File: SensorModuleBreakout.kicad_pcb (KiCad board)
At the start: 2 copper layers, 41 x 42.7 mm, 23 parts, among them J1 Conn_01x04, J2 Conn_ST_STDC14, J3 Conn_01x03, J4 Conn_01x10, J5 Conn_01x15, U1 STM32U031C8Tx

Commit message: V2
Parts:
- removed FB1: 120R, Inductor_SMD:L_0603_1608Metric
- removed S1: USEQGSEAC82180, USEQGS:USEQGSEAC82180
- added C10: 100n, Capacitor_SMD:C_0402_1005Metric, F.Cu at (130.5, 65.0)
- added C12: 100n, Capacitor_SMD:C_0402_1005Metric, F.Cu at (135.9, 93.2)
- added C9: 100n, Capacitor_SMD:C_0402_1005Metric, F.Cu at (124.9, 60.6)
- added H1: MountingHole_Pad, MountingHole:MountingHole_3.2mm_M3_DIN965_Pad, F.Cu at (106.0, 56.0)
- added H2: MountingHole_Pad, MountingHole:MountingHole_3.2mm_M3_DIN965_Pad, F.Cu at (154.0, 56.0)
- added H3: MountingHole_Pad, MountingHole:MountingHole_3.2mm_M3_DIN965_Pad, F.Cu at (106.0, 104.0)
- added H4: MountingHole_Pad, MountingHole:MountingHole_3.2mm_M3_DIN965_Pad, F.Cu at (154.0, 104.0)
- added R4: 2M, Resistor_SMD:R_0603_1608Metric, F.Cu at (118.0, 90.3)
- added R5: 1M, Resistor_SMD:R_0402_1005Metric, F.Cu at (118.0, 92.9)
- added R6: 220r, Resistor_SMD:R_0402_1005Metric, F.Cu at (120.5, 97.1)
- added REF**: ToolingHole_1.152mm, MountingHole:ToolingHole_1.152mm, F.Cu at (157.2, 62.0)
- added REF**: ToolingHole_1.152mm, MountingHole:ToolingHole_1.152mm, F.Cu at (103.1, 61.9)
- added REF**: ToolingHole_1.152mm, MountingHole:ToolingHole_1.152mm, F.Cu at (156.9, 97.5)
- added U2: SHT4x, Sensor_Humidity:Sensirion_DFN-4_1.5x1.5mm_P0.8mm_SHT4x_NoCentralPad, F.Cu at (124.9, 62.4)
- added U3: STC31-C-R3, STC31_C_R3:XDCR_STC31-C-R3, F.Cu at (130.0, 62.0)
- added U4: LPS22DF, Package_LGA:ST_HLGA-10_2x2mm_P0.5mm_LayoutBorder3x2y, F.Cu at (135.3, 62.4)
- C5: value 10n -> 100n
- C6: value 1u -> 10n
- C8: value 100n -> 1u
- D1: footprint LED_SMD:LED_0402_1005Metric -> LED_SMD:LED_0603_1608Metric
- J1: value Conn_01x04 -> Conn_ST_STDC14; footprint Connector_JST:JST_XH_B4B-XH-A_1x04_P2.50mm_Vertical -> Connector_PinHeader_1.27mm:PinHeader_2x07_P1.27mm_Vertical
- J2: value Conn_ST_STDC14 -> Conn_01x10; footprint Connector_PinHeader_1.27mm:PinHeader_2x07_P1.27mm_Vertical_SMD -> Connector_PinHeader_2.54mm:PinHeader_1x10_P2.54mm_Vertical
- J3: value Conn_01x03 -> Conn_01x15; footprint Connector_JST:JST_XH_B3B-XH-A_1x03_P2.50mm_Vertical -> Connector_PinHeader_2.54mm:PinHeader_1x15_P2.54mm_Vertical
- J4: value Conn_01x10 -> Conn_01x03; footprint Connector_PinHeader_2.54mm:PinHeader_1x10_P2.54mm_Vertical -> Connector_JST:JST_XH_B3B-XH-A_1x03_P2.50mm_Vertical
- J5: value Conn_01x15 -> Conn_01x04; footprint Connector_PinHeader_2.54mm:PinHeader_1x15_P2.54mm_Vertical -> Connector_JST:JST_XH_B4B-XH-A_1x04_P2.50mm_Vertical
- JP1: value JP -> Jumper_2_Open
- JP2: value Jumper_2_Open -> JP
- R1, R2, R3: value 1k5 -> 10k
- moved J3 75.1 mm to (154.0, 61.9)
- moved J4 48.5 mm to (113.7, 104.0)
- moved J1 41.9 mm to (140.4, 105.2), turned to 90 degrees
- moved J5 40.8 mm to (126.9, 104.1)
- moved R3 38.3 mm to (131.0, 78.9), turned to 180 degrees
- moved JP2 32.4 mm to (120.3, 99.5)
- moved C6 31.2 mm to (125.2, 89.1), turned to 90 degrees
- moved C7 30.3 mm to (124.0, 89.1), turned to 90 degrees
- moved C1 28.4 mm to (127.8, 81.3)
- moved C2 28.2 mm to (128.2, 82.7)
- moved U1 28.0 mm to (131.0, 88.5)
- moved C4 28.0 mm to (133.9, 94.2)
- moved C3 28.0 mm to (136.8, 85.5)
- moved C5 27.5 mm to (125.2, 84.9)
- moved D1 26.8 mm to (118.1, 97.1)
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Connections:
- C11 pad 1: Net-(S1-CAP) -> +3V3
- C5 pad 1: +3V3A -> +3V3
- C6 pad 1: +3V3A -> +3V3
- C8 pad 1: VBAT -> +3V3
- J1 pad 1: TX -> unconnected-(J1-NC-Pad1)
- J1 pad 2: RX -> unconnected-(J1-NC-Pad2)
- J1 pad 3: WKE -> +3V3
- J1 pad 4: RDY -> JTMS/SWDIO
- J2 pad 1: unconnected-(J2-NC-Pad1) -> +3V3
- J2 pad 10: unconnected-(J2-JTDI/NC-Pad10) -> PA1
- J2 pad 2: unconnected-(J2-NC-Pad2) -> GND
- J2 pad 3: +3V3 -> PB4
- J2 pad 4: JTMS/SWDIO -> PA15
- J2 pad 5: GND -> PA12
- J2 pad 6: JTCK_SWCLK -> PA11
- J2 pad 7: GND -> PB8
- J2 pad 8: JTDO/SWO -> PB9
- J2 pad 9: unconnected-(J2-JRCLK/NC-Pad9) -> PA8
- J3 pad 1: VBAT -> SDA
- J3 pad 2: GND -> SCL
- J3 pad 3: +3V3 -> PB15
- J4 pad 1: +3V3 -> VBAT
- J4 pad 3: PB8 -> +3V3
- J5 pad 1: +3V3 -> CC_TX
- J5 pad 2: GND -> CC_RX
- J5 pad 3: unconnected-(J5-Pin_3-Pad3) -> CC_WKE
- J5 pad 4: PA8 -> CC_RDY
- JP1 pad 1: Net-(JP1-A) -> +3V3
- JP1 pad 2: +3V3 -> /BOOT0
- JP2 pad 1: +3V3 -> Net-(JP2-A)
- JP2 pad 2: VBAT -> +3V3
- R1 pad 1: +3V3 -> /BOOT0
- R1 pad 2: SCL -> GND
- R2 pad 2: SDA -> SCL
- R3 pad 1: Net-(D1-A) -> +3V3
- R3 pad 2: Net-(JP1-A) -> SDA
- U1 pad 1: VBAT -> +3V3
- U1 pad 10: PA0 -> Net-(U1-PA0)
- U1 pad 12: TX -> CC_TX
- U1 pad 13: RX -> CC_RX
- U1 pad 14: WKE -> CC_WKE
- U1 pad 15: RDY -> CC_RDY
- U1 pad 2: PC13 -> unconnected-(U1-PC13-Pad2)
- U1 pad 3: PC14 -> unconnected-(U1-PC14-Pad3)
- U1 pad 30: SCL -> VCP_TX
- U1 pad 31: SDA -> VCP_RX
- U1 pad 32: INT -> PA11
- U1 pad 33: CS -> PA12
- U1 pad 38: unconnected-(U1-PA15-Pad38) -> PA15
- U1 pad 4: PC15 -> unconnected-(U1-PC15-Pad4)
- U1 pad 40: unconnected-(U1-PB4-Pad40) -> PB4
- U1 pad 41: unconnected-(U1-PB5-Pad41) -> INT
- U1 pad 42: VCP_TX -> SCL
- U1 pad 43: VCP_RX -> SDA
- U1 pad 44: unconnected-(U1-PF3-Pad44) -> /BOOT0
- U1 pad 5: PF0 -> unconnected-(U1-PF0-Pad5)
- U1 pad 9: +3V3A -> +3V3
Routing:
- net +3V3: track 256.7 -> 30.0 mm, vias 4 -> 11
- net SDA: track 8.18 -> 66.7 mm
- net SCL: track 11.6 -> 64.1 mm, vias 0 -> 3
- net PA15: track 0.00 -> 40.4 mm, vias 0 -> 1
- net PB4: track 0.00 -> 39.8 mm, vias 0 -> 2
- net PA11: track 0.00 -> 36.3 mm
- net PA12: track 0.00 -> 35.9 mm, vias 0 -> 3
- net /BOOT0: track 0.00 -> 33.6 mm, vias 0 -> 2
- net NRST: track 64.1 -> 30.8 mm
- net JTDO/SWO: track 10.5 -> 34.7 mm, vias 0 -> 1
- net VCP_RX: track 15.8 -> 39.2 mm, vias 0 -> 2
- net VCP_TX: track 11.5 -> 34.7 mm, vias 0 -> 2
- net VBAT: track 38.9 -> 17.5 mm, vias 2 -> 0
- net JTCK_SWCLK: track 10.4 -> 31.4 mm, vias 0 -> 1
- net PB14: track 19.9 -> 39.0 mm, vias 0 -> 2
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- added copper zone on In2.Cu, net +3V3
- added copper zone on In1.Cu, net GND
- removed copper zone on B.Cu, net GND
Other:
- board size 41 x 42.7 mm -> 60 x 60 mm
- copper layers 2 -> 4
- board text added: "CottonCandy"
- board text added: "PA11"
- board text added: "PA12"
- board text added: "PA15"
- board text added: "PA6"
- board text added: "PB4"
- board text added: "SCL"
- board text added: "SDA"
- board text added: "Temp, Humidity, Pressure, CO2 Sensor Module"
- board text added: "UART1_RX"
- board text added: "UART1_TX"
- board text removed: "+"
- board text removed: "-"
- board text removed: "NC"
- board text removed: "PA0"
- board text removed: "PC13"
- board text removed: "PC14"
- board text removed: "PC15"
- board text removed: "PF0"
- board text removed: "PWR LED"
- board text removed: "STMU0 Sensor Module"
- board text removed: "VBAT Short"

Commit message: update
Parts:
- removed U4: LPS22DF, Package_LGA:ST_HLGA-10_2x2mm_P0.5mm_LayoutBorder3x2y
- added U5: MS5607-02BA, Package_LGA:LGA-8_3x5mm_P1.25mm, F.Cu at (136.2, 61.7)
- moved C11 1.82 mm to (133.8, 61.8), turned to -90 degrees
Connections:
- U1 pad 41: INT -> unconnected-(U1-PB5-Pad41)
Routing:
- net INT: track 25.8 -> 0.00 mm, vias 2 -> 0
- net SCL: track 64.1 -> 68.4 mm
- net SDA: track 66.7 -> 68.7 mm
- net GND: track 32.4 -> 34.3 mm, vias 20 -> 21
- net +3V3: track 30.0 -> 29.1 mm

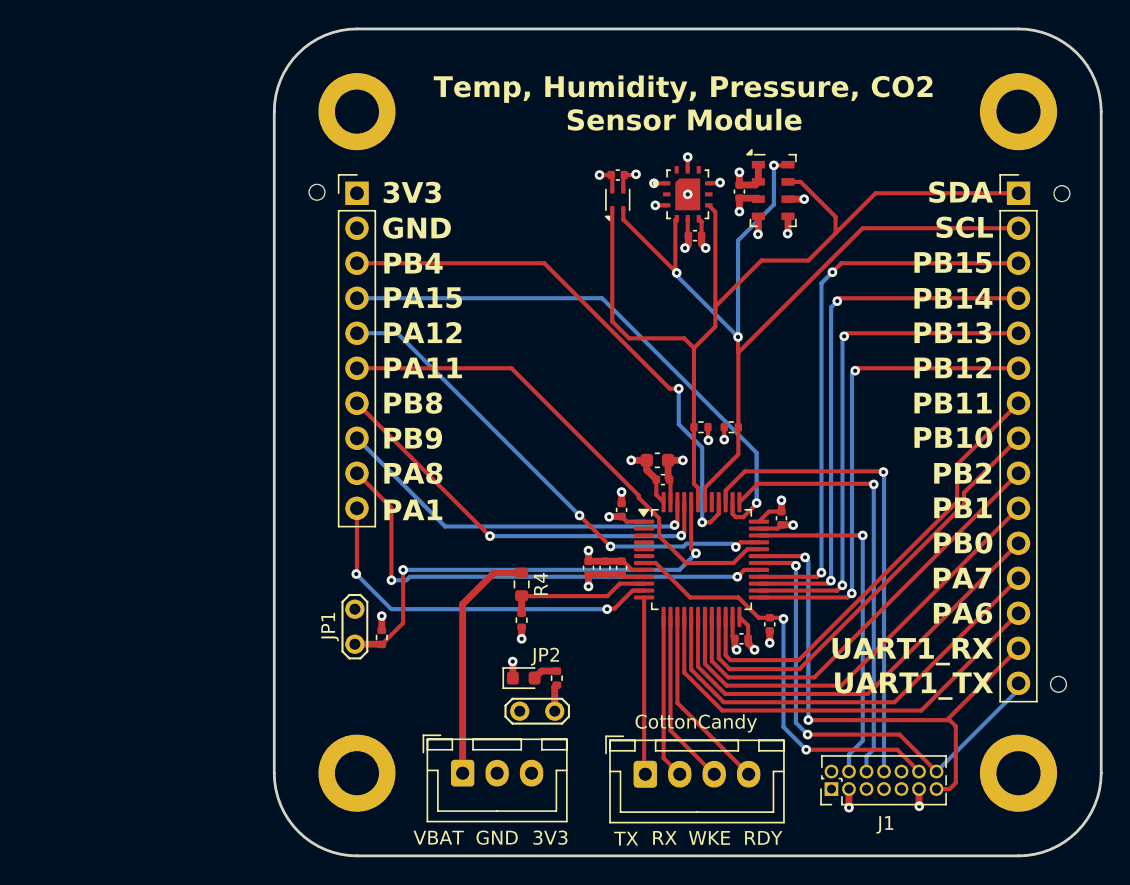
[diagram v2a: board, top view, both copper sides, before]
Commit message: Fix some rotation errors and minor cleanup
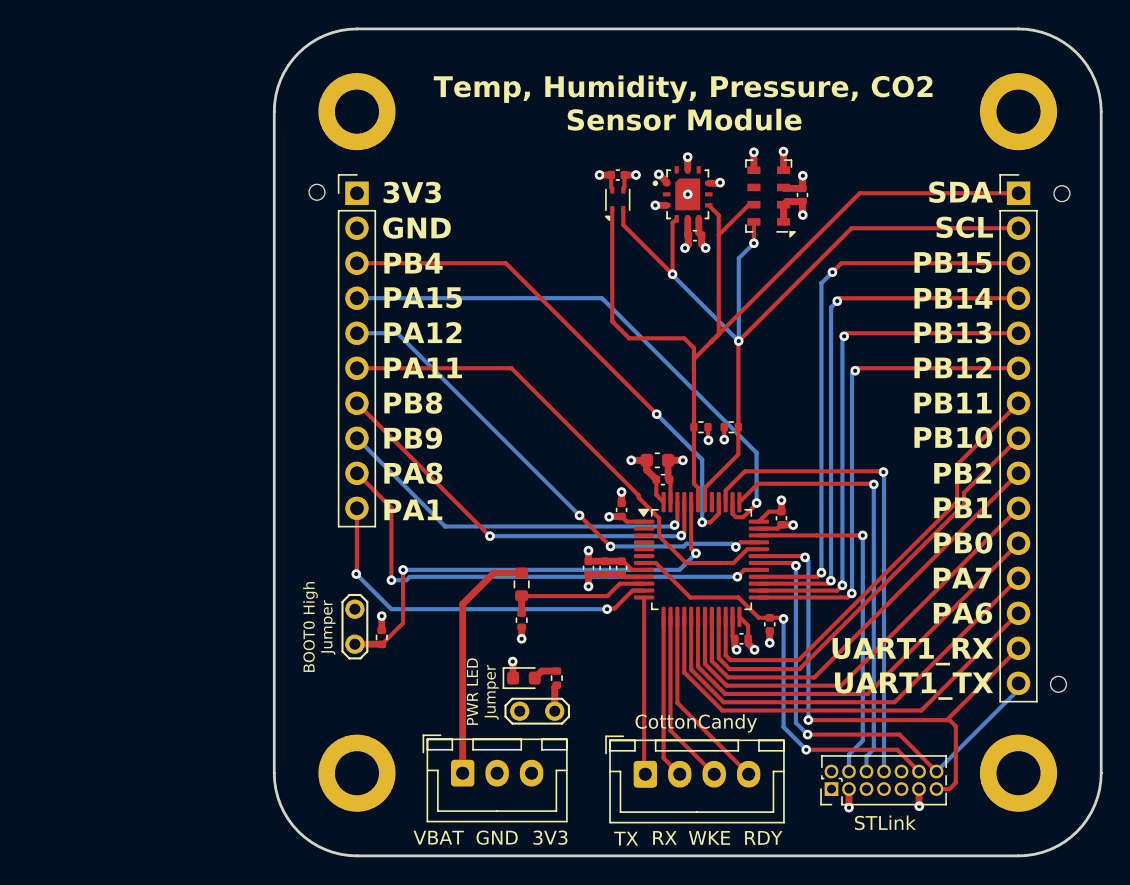
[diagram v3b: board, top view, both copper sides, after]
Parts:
- moved C11 4.58 mm to (138.3, 62.0), turned to 90 degrees
- moved U5 0.52 mm to (135.9, 62.1), turned to 180 degrees
- renumbered J1 to STLink
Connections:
- U5 pad 6: GND -> unconnected-(U5-SDO-Pad6)
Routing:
- net SCL: track 68.4 -> 62.8 mm
- net PB4: track 39.8 -> 37.8 mm
- net GND: track 34.3 -> 33.0 mm, vias 21 -> 20
- net SDA: track 68.7 -> 69.5 mm
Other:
- board text added: "BOOT0 High Jumper"
- board text added: "PWR LED Jumper"
